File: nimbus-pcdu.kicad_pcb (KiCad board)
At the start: 4 copper layers, 61.9 x 61.9 mm, 0 parts

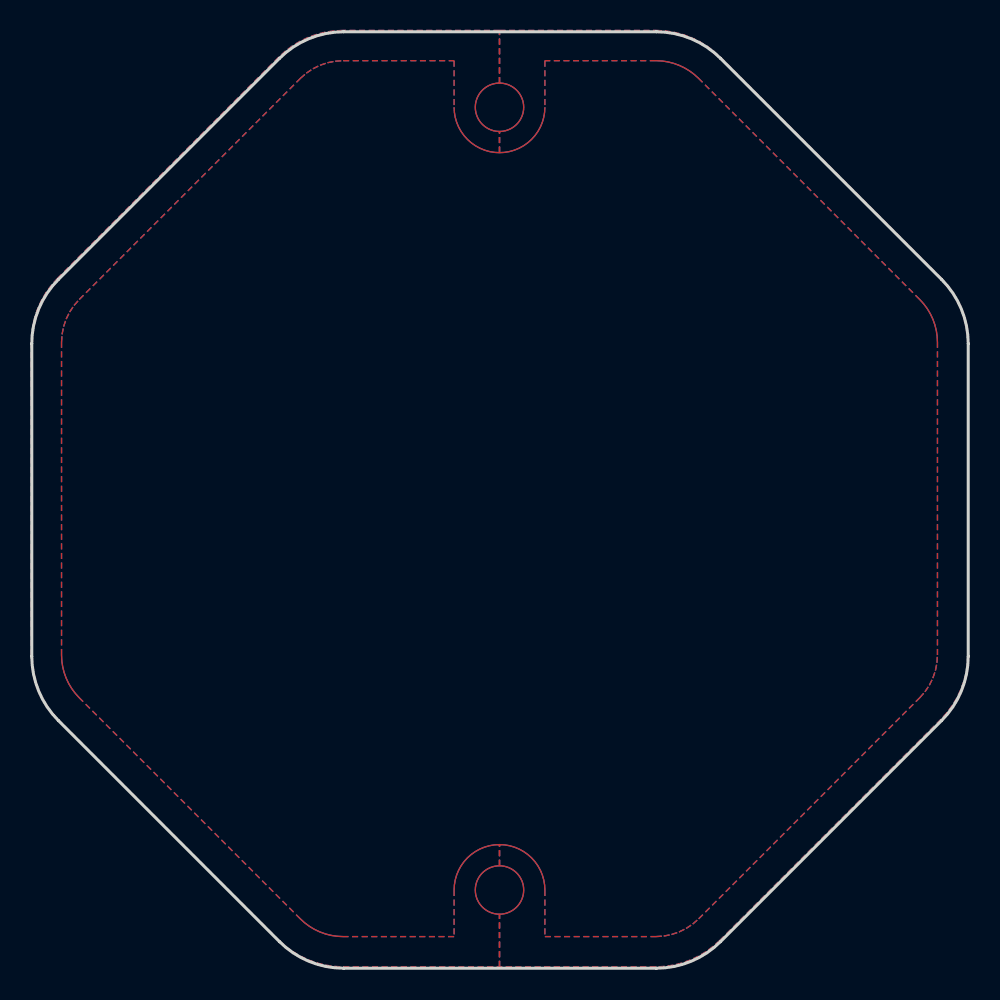
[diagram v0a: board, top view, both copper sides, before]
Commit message: Add interboard connector, mounting holes and BMS IC. Chassis connection still missing
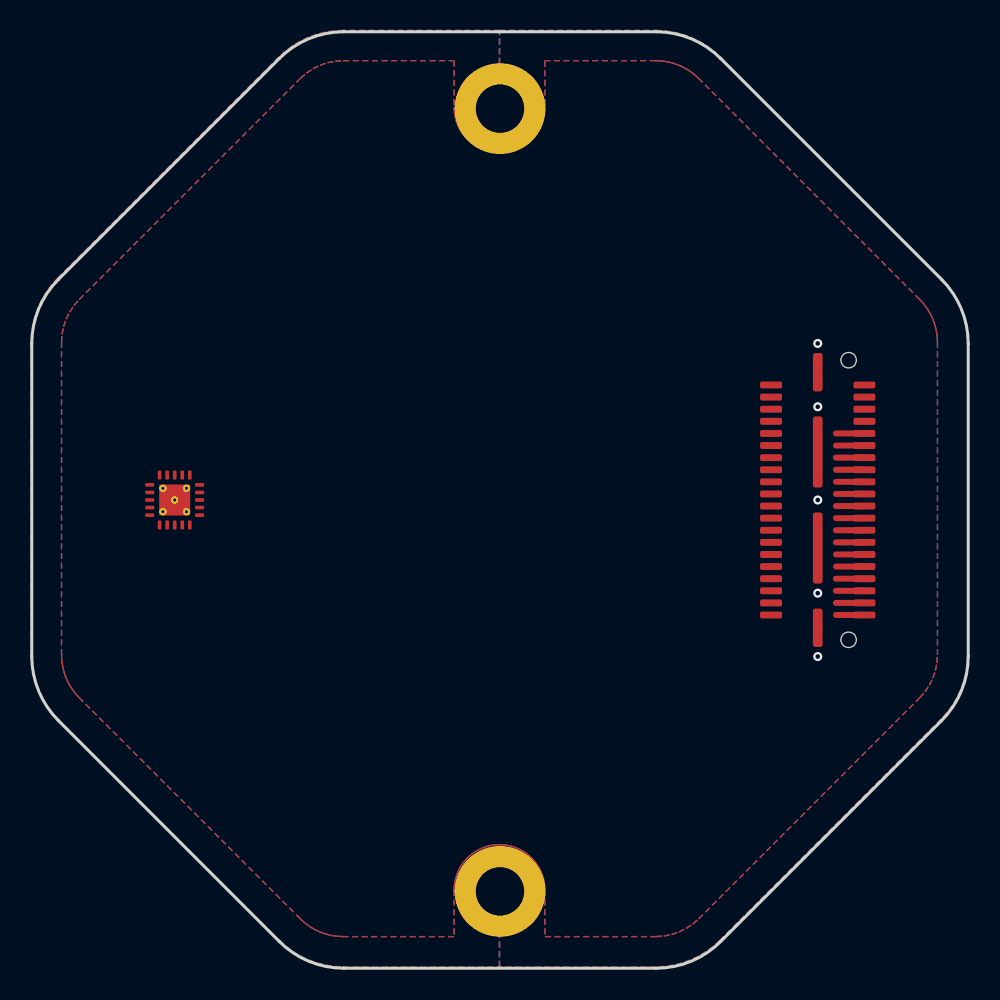
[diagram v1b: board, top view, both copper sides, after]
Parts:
- added J1: QTE-020-03-L-D-A, connector:QTE-020-03-L-D-A, F.Cu at (231.0, 148.5)
- added REF**: Mounting_Hole_M3, layout:Mounting_Hole_M3, F.Cu at (210.0, 122.6)
- added REF**: Mounting_Hole_M3, layout:Mounting_Hole_M3, F.Cu at (210.0, 174.4)
- added U1: BQ76905RGRR, integrated_semiconductor:BQ76905RGRR, F.Cu at (188.5, 148.5)
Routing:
- net /PE0: track 0.00 -> 1.89 mm
- net /PD8: track 0.00 -> 1.89 mm
- net /PD7: track 0.00 -> 1.89 mm
- net /PB14: track 0.00 -> 1.89 mm
- net /PB12: track 0.00 -> 1.89 mm
- net /PB8: track 0.00 -> 1.89 mm
- net /PB5: track 0.00 -> 1.88 mm
- net /I2C1_SDA: track 0.00 -> 1.88 mm
- net /PE1: track 0.00 -> 1.88 mm
- net /PB13: track 0.00 -> 1.88 mm
- net /PB9: track 0.00 -> 1.88 mm
- net /PB4: track 0.00 -> 1.88 mm
- net /PD6: track 0.00 -> 1.88 mm
- net /PD9: track 0.00 -> 1.88 mm
- net /I2C1_SCL: track 0.00 -> 1.88 mm
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- added copper zone on B.Cu, net GND
- added copper zone on F.Cu, net GND
- added copper zone on In1.Cu, net GND
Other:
- board text added: "J2"

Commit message: Add initial BMS component selection
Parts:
- added C1: 1μF, passive:C_0805_Density_Least, F.Cu at (197.5, 140.7)
- added C10: 1μF, passive:C_0805_Density_Least, F.Cu at (201.8, 131.8)
- added C11: 1μF, passive:C_0805_Density_Least, F.Cu at (201.8, 134.5)
- added C2: 220nF, passive:C_0603_Density_Least, F.Cu at (188.5, 131.6)
- added C3: 220nF, passive:C_0603_Density_Least, F.Cu at (188.5, 133.8)
- added C4: 220nF, passive:C_0603_Density_Least, F.Cu at (188.5, 136.0)
- added C5: 220nF, passive:C_0603_Density_Least, F.Cu at (188.5, 138.2)
- added C6: 220nF, passive:C_0603_Density_Least, F.Cu at (191.9, 131.6)
- added C7: 100nF, passive:C_0603_Density_Least, F.Cu at (191.9, 133.8)
- added C8: 100pF, passive:C_0603_Density_Least, F.Cu at (191.9, 136.0)
- added C9: 100pF, passive:C_0603_Density_Least, F.Cu at (191.9, 138.2)
- added R1: 10Ω, passive:R_0603_Density_Least, F.Cu at (195.3, 131.6)
- added R2: 10Ω, passive:R_0603_Density_Least, F.Cu at (195.3, 133.8)
- added R3: 10Ω, passive:R_0603_Density_Least, F.Cu at (195.3, 136.0)
- added R4: 10Ω, passive:R_0603_Density_Least, F.Cu at (195.3, 138.2)
- added R5: 10Ω, passive:R_0603_Density_Least, F.Cu at (198.7, 131.6)
- added R6: 100Ω, passive:R_0603_Density_Least, F.Cu at (198.7, 133.8)
- added R7: 100Ω, passive:R_0603_Density_Least, F.Cu at (198.7, 136.0)
- added R8: 100Ω, passive:R_0603_Density_Least, F.Cu at (198.7, 138.2)
- added R9: 1mΩ, passive:CRE2512-FZ-R001E-2, F.Cu at (191.2, 142.0)
- added U2: BQ25730RSNR, integrated_semiconductor:BQ25730RSNR, F.Cu at (196.4, 148.5)
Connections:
- U1 pad 1: unconnected-(U1-VC3A-Pad1) -> Net-(U1-VC2)
- U1 pad 12: unconnected-(U1-SCL-Pad12) -> /I2C1_SCL
- U1 pad 13: unconnected-(U1-SDA-Pad13) -> /I2C1_SDA
- U1 pad 15: unconnected-(U1-REGOUT-Pad15) -> Net-(U1-REGOUT)
- U1 pad 16: unconnected-(U1-REGSRC-Pad16) -> Net-(U1-REGSRC)
- U1 pad 17: VBAT -> Net-(U1-BAT)
- U1 pad 18: unconnected-(U1-VC5-Pad18) -> Net-(U1-VC5)
- U1 pad 19: unconnected-(U1-VC4A-Pad19) -> Net-(U1-VC4A)
- U1 pad 2: unconnected-(U1-VC3B-Pad2) -> Net-(U1-VC2)
- U1 pad 20: unconnected-(U1-VC4B-Pad20) -> Net-(U1-VC4A)
- U1 pad 3: unconnected-(U1-VC2-Pad3) -> Net-(U1-VC2)
- U1 pad 4: unconnected-(U1-VC1-Pad4) -> Net-(U1-VC1)
- U1 pad 5: unconnected-(U1-VC0-Pad5) -> Net-(U1-VC0)
- U1 pad 6: unconnected-(U1-SRP-Pad6) -> Net-(U1-SRP)
- U1 pad 7: unconnected-(U1-SRN-Pad7) -> Net-(U1-SRN)
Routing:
- net /PE0: track 1.89 -> 0.00 mm
- net /PD8: track 1.89 -> 0.00 mm
- net /PD7: track 1.89 -> 0.00 mm
- net /PB14: track 1.89 -> 0.00 mm
- net /PB12: track 1.89 -> 0.00 mm
- net /PB8: track 1.89 -> 0.00 mm
- net /PB5: track 1.88 -> 0.00 mm
- net /I2C1_SDA: track 1.88 -> 0.00 mm
- net /PE1: track 1.88 -> 0.00 mm
- net /PB13: track 1.88 -> 0.00 mm
- net /PB9: track 1.88 -> 0.00 mm
- net /PB4: track 1.88 -> 0.00 mm
- net /PD6: track 1.88 -> 0.00 mm
- net /PD9: track 1.88 -> 0.00 mm
- net /I2C1_SCL: track 1.88 -> 0.00 mm
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- added copper zone on In2.Cu, net +3.3V
